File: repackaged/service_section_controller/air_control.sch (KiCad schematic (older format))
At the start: 18 parts, among them Q901 SSM3K333R, Q902 SSM3K333R

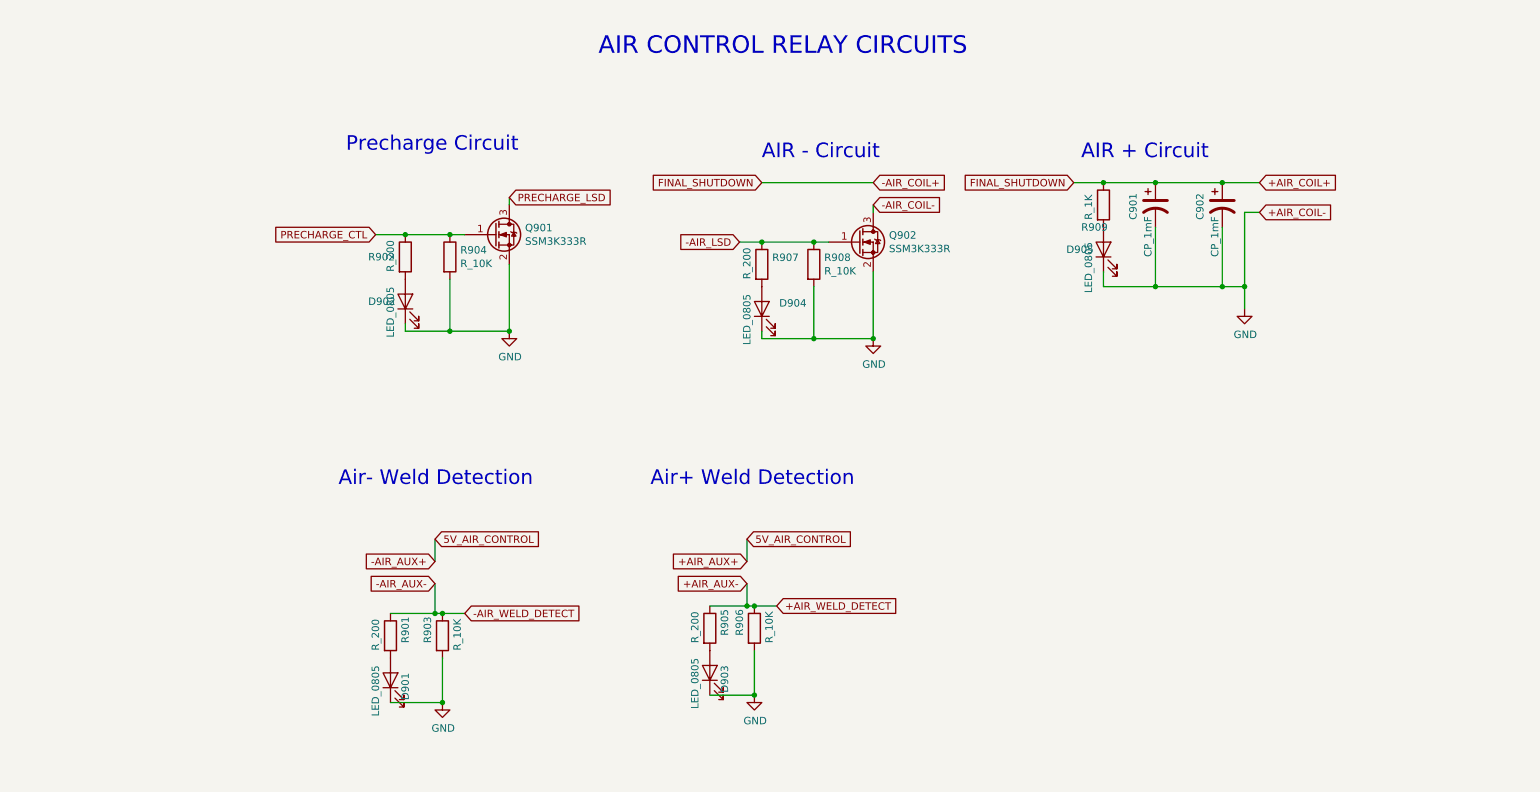
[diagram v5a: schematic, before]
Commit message: added test points and re-did schematic with new traces.
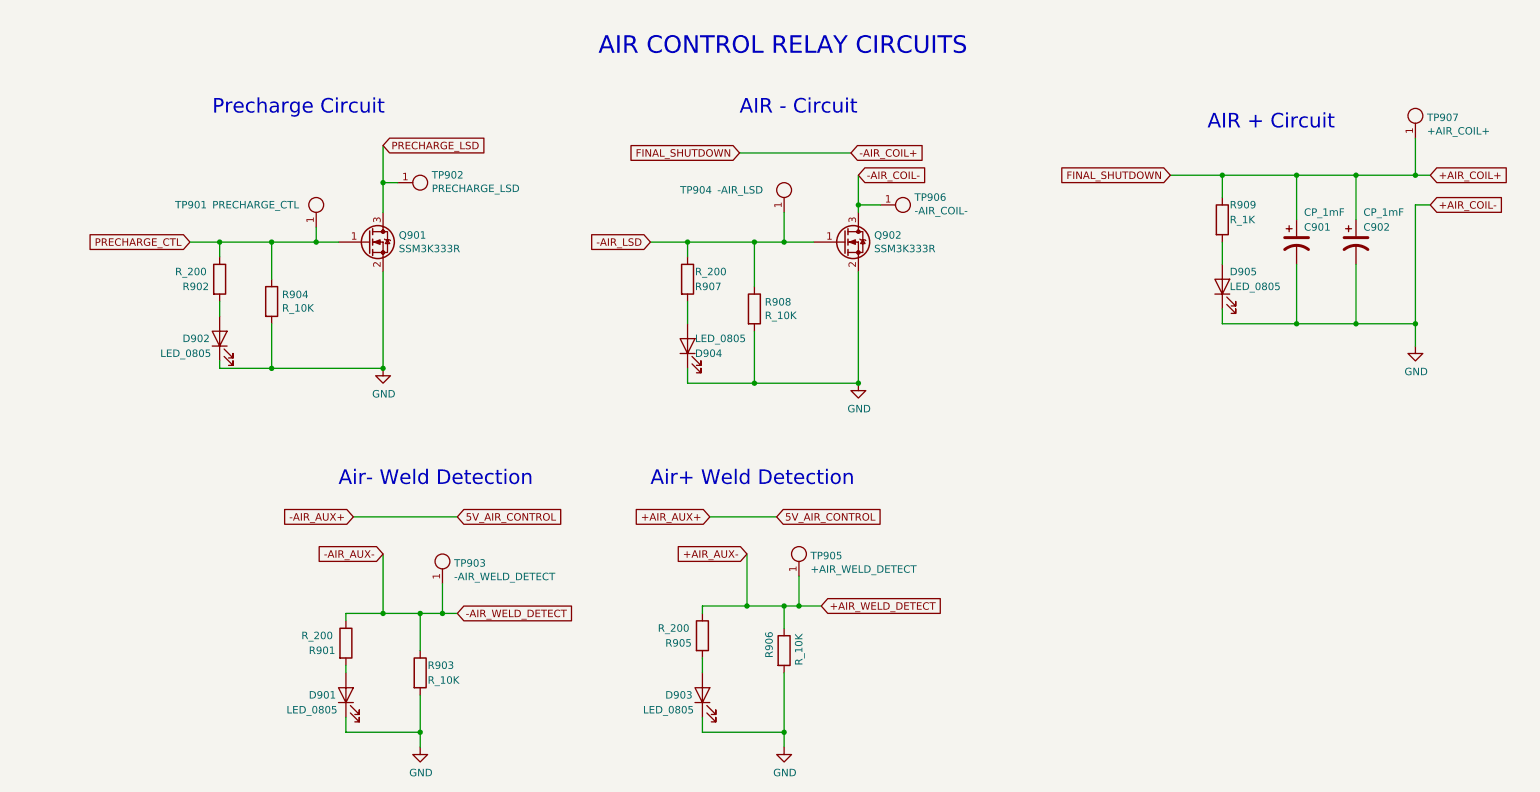
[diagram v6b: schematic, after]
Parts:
- added TP901: PRECHARGE_CTL, TestPoint:TestPoint_Pad_D1.0mm, symbol formula:Test_Point_SMD
- added TP902: PRECHARGE_LSD, TestPoint:TestPoint_Pad_D1.0mm, symbol formula:Test_Point_SMD
- added TP903: -AIR_WELD_DETECT, TestPoint:TestPoint_Pad_D1.0mm, symbol formula:Test_Point_SMD
- added TP904: -AIR_LSD, TestPoint:TestPoint_Pad_D1.0mm, symbol formula:Test_Point_SMD
- added TP905: +AIR_WELD_DETECT, TestPoint:TestPoint_Pad_D1.0mm, symbol formula:Test_Point_SMD
- added TP906: -AIR_COIL-, TestPoint:TestPoint_Pad_D1.0mm, symbol formula:Test_Point_SMD
- added TP907: +AIR_COIL+, TestPoint:TestPoint_Pad_D1.0mm, symbol formula:Test_Point_SMD
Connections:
- net +AIR_AUX-: now also TP905.1
- net +AIR_COIL+: now also TP907.1
- net -AIR_AUX-: now also TP903.1
- net -AIR_COIL-: now also TP906.1
- net -AIR_LSD: now also TP904.1
- net PRECHARGE_CTL: now also TP901.1
- net PRECHARGE_LSD: now also TP902.1
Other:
- moved on the sheet: C901, C902, D901, D902, D903, D904, D905, Q901, Q902, R901, R902, R903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
